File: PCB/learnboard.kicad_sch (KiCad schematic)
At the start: 59 parts, among them SW1 SW_Push, SW10 SW_Push, SW11 SW_Push, SW12 SW_Push, SW13 SW_Push, SW14 SW_Push, SW15 SW_Push, SW16 SW_Push, SW17 RotaryEncoder_Switch_MP, SW2 SW_Push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

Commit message: Updated the zine and the readme abit.
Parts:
- U1: footprint Package_SO:TSSOP-20_4.4x6.5mm_P0.65mm -> Package_CSP:Nexperia_WLCSP-15_2.37x1.17mm_Layout6x3_P0.4mmP0.8mm

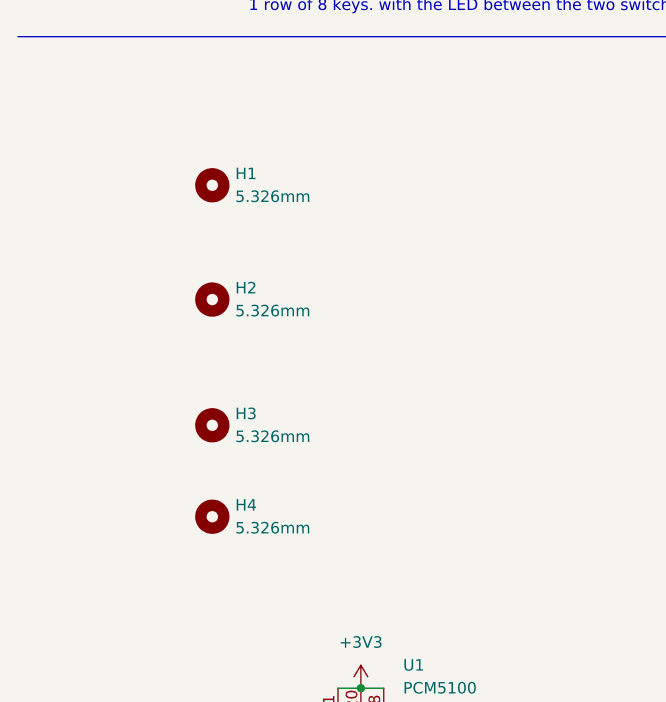
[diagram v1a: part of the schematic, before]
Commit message: Updated pcb to use the right diode footprints
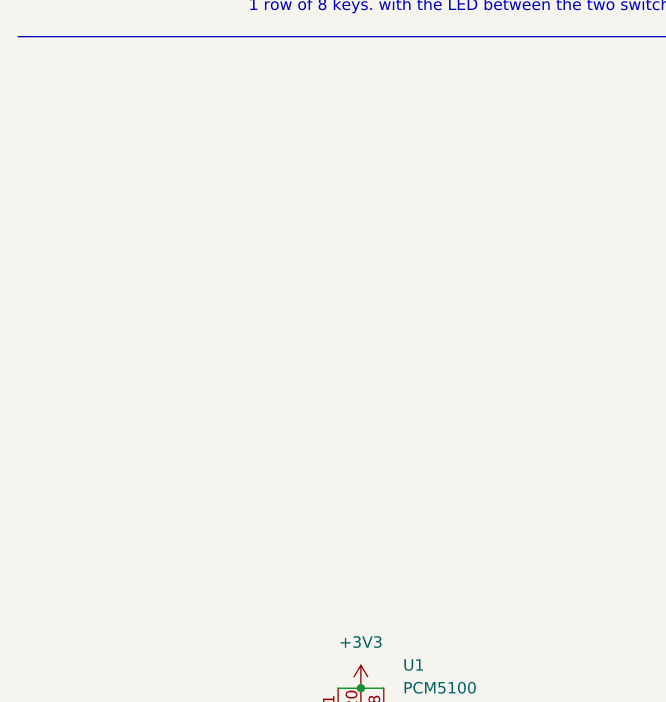
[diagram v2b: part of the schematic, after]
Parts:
- removed H1, H2, H3, H4: 5.326mm, MountingHole:MountingHole_5.5mm, symbol Mechanical:MountingHole
- D1, D10, D11, D12, D13, D14, D15, D2, D3, D4, D5, D6, D7, D8, D9: footprint Diode_SMD:D_0201_0603Metric -> Diode_THT:D_T-1_P10.16mm_Horizontal
